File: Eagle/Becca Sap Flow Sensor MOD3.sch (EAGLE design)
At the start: 59 parts, among them U1 V_REG_317SMD, U2 BORON, U6 RFM69HCW, U7 74HC4050D, U8 AP2112K-3.3, X2 USB Type C, X4 BQ24074, X5 uFL/SMA

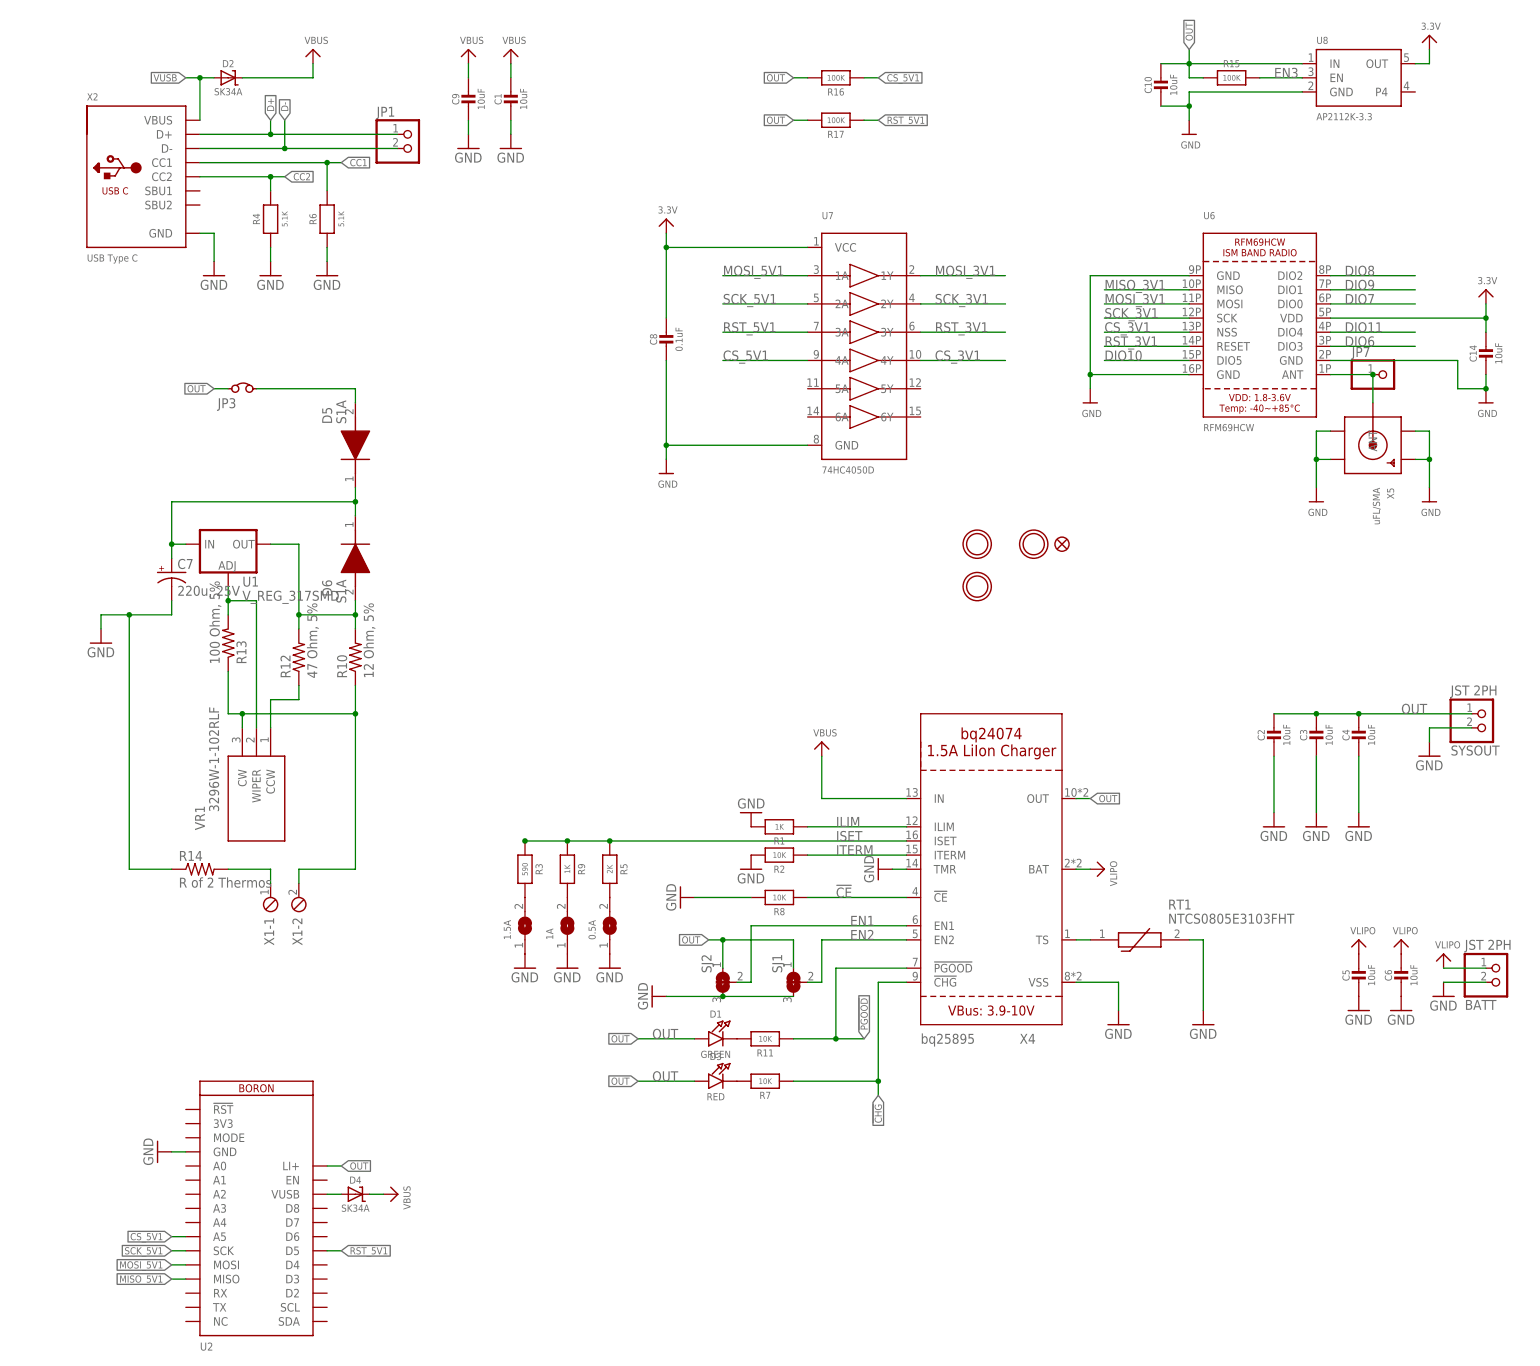
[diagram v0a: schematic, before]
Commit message: Amended git ignore, also adding most recent sch
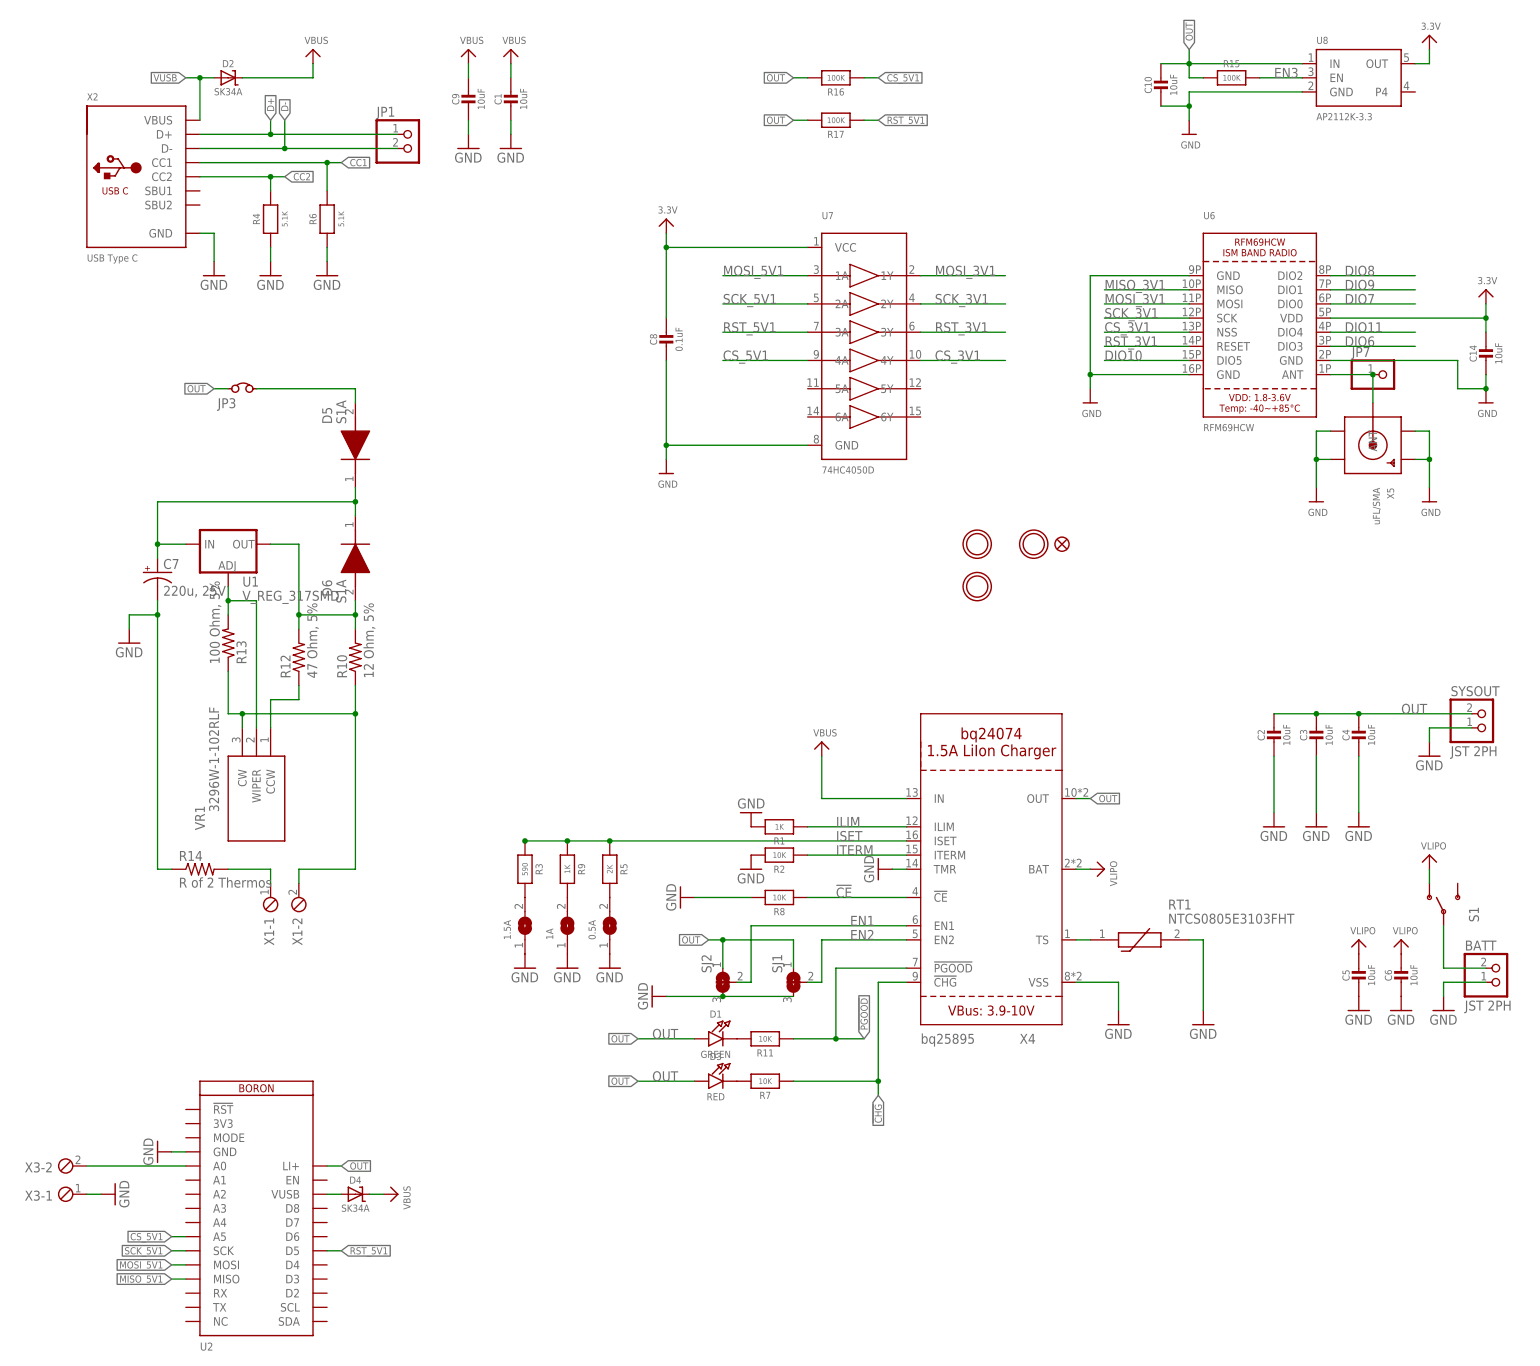
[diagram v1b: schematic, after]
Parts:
- added S1: (no value), SparkFun-Retired:SWITCH-SPDTSMD
- added X3: (no value), con-phoenix-254:MPT2
- BATT, SYSOUT: device adafruit:JST_2PIN-SMT-RA -> adafruit:JST_2PIN-THM-RA
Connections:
- new net N$17: U2.A0, X3-2.1
- new net N$2: BATT.1, S1.P
- net GND: now also BATT.2, SYSOUT.2, X3-1.1; no longer BATT.1, SYSOUT.1
- net OUT: now also SYSOUT.1; no longer SYSOUT.2
- net VLIPO: now also S1.O; no longer BATT.2
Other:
- moved on the sheet: BATT, C7, SYSOUT
